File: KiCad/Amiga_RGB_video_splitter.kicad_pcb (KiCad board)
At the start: 4 copper layers, 57.5 x 60 mm, 15 parts, among them J1 DB23_Female-Connector, J2 DB15_Female_HighDensity_Mount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, J3 KMDGX-9S-BS-1, J4 PJ-320A, U1 THS7374IPWR, U2 74HCT2G17

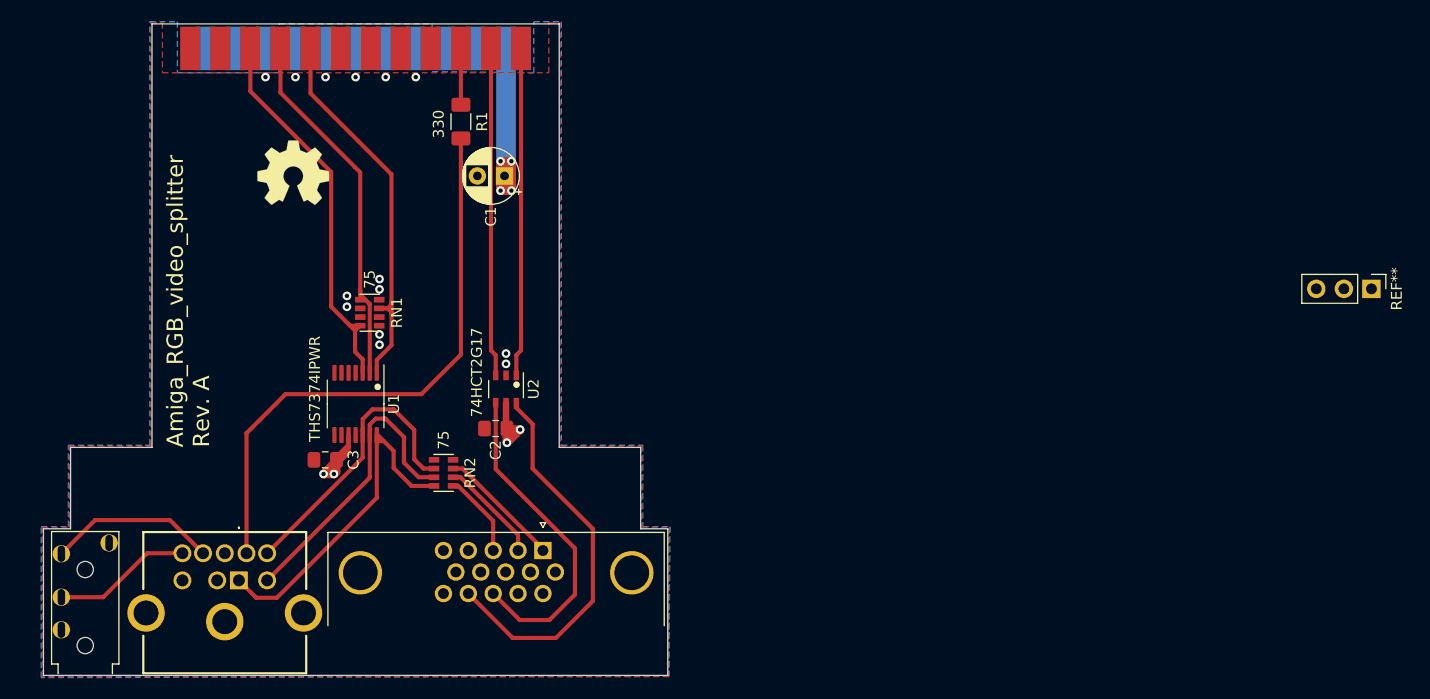
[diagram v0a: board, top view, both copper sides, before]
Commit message: Add 10k pull-up resistor R2 for BYPASS signal going to MSS22D18 3-Pin slide toggle switch
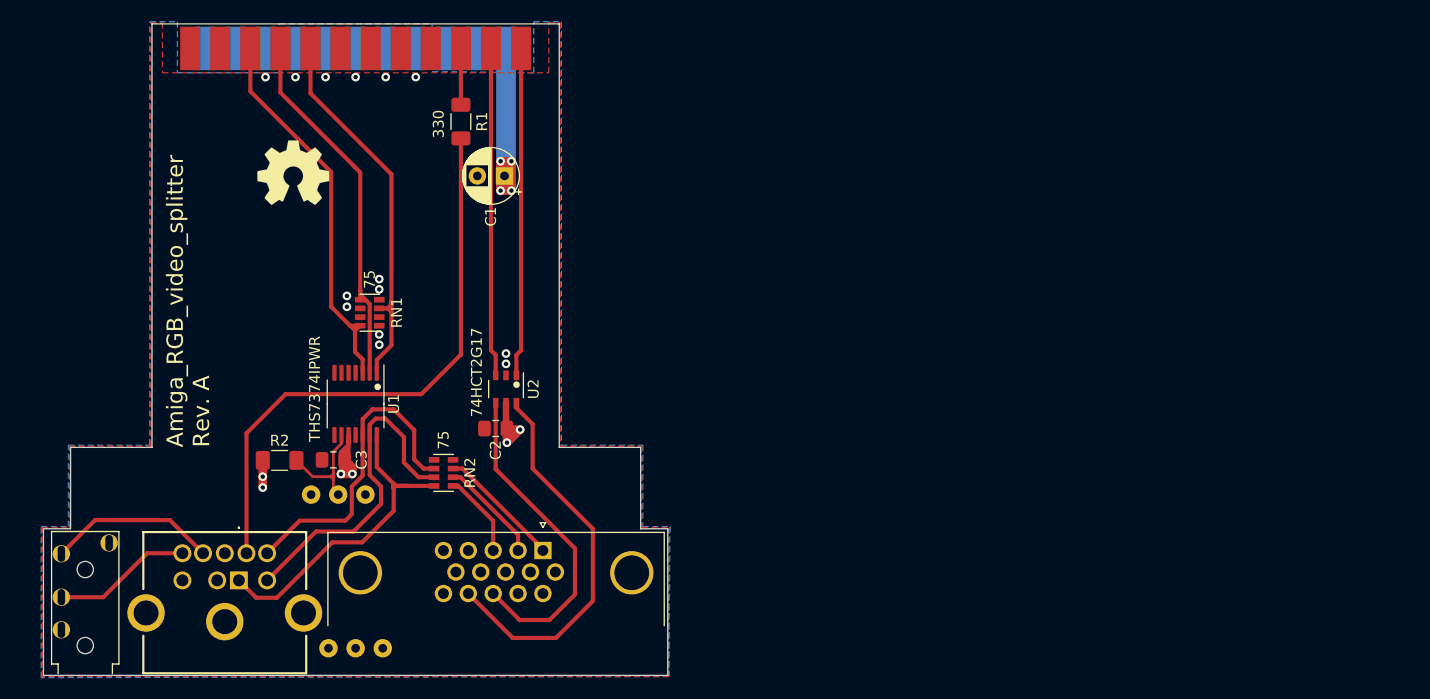
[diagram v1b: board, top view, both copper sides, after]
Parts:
- removed the REF** at (241.2, 109.4)
- added J5: Conn_01x03, Amiga_RGB_video_splitter:PinHeader_1x03_P2.5mm_Vertical, B.Cu at (147.7, 142.5)
- added J5: Conn_01x03, Amiga_RGB_video_splitter:PinHeader_1x03_P2.5mm_Vertical, F.Cu at (146.1, 128.3)
- added R2: 10k, Resistor_SMD:R_1206_3216Metric_Pad1.30x1.75mm_HandSolder, F.Cu at (140.7, 125.2)
- R1: value R_Small -> 330
- moved C3 0.75 mm to (145.7, 125.2)
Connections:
- U1 pad 9: BYPASS -> /BYPASS
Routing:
- net /BYPASS: track 0.00 -> 10.8 mm
- net GREEN: track 28.0 -> 30.9 mm
- net VCC: track 82.5 -> 85.0 mm, vias 8 -> 10
- net RED: track 26.8 -> 29.2 mm

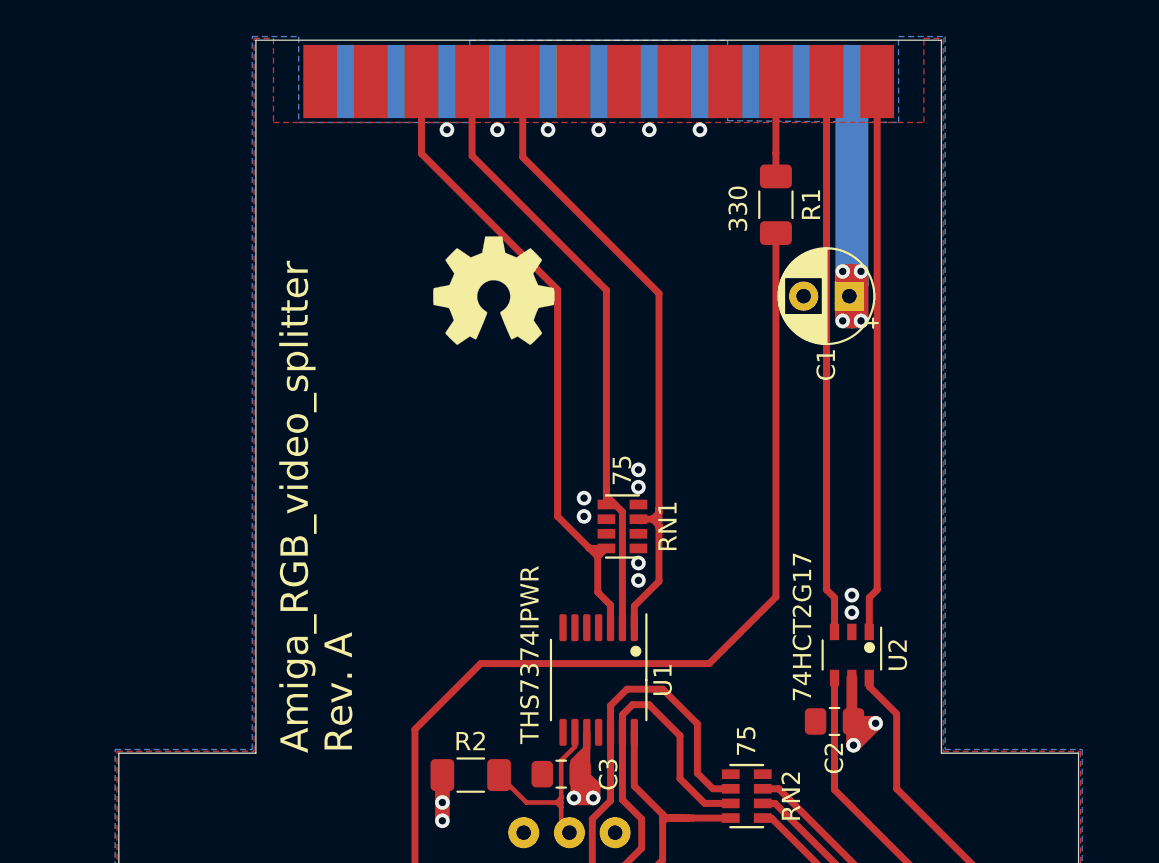
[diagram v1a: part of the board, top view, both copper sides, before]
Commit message: Add U3 (74HCT2G14) and R3,R4,C4,C5 to the design
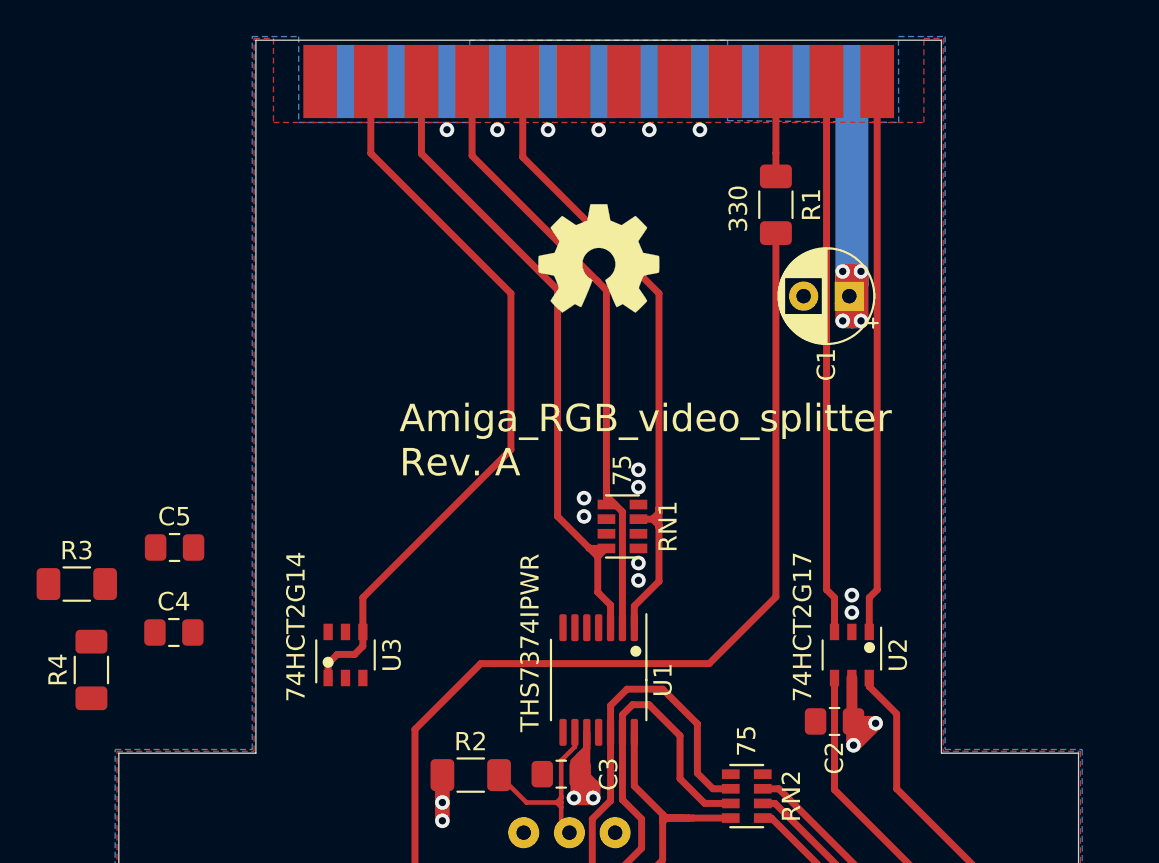
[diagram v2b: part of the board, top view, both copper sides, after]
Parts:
- removed the J5 at (147.7, 142.5)
- added C4: 0.1uF, Capacitor_SMD:C_0805_2012Metric_Pad1.18x1.45mm_HandSolder, F.Cu at (124.5, 117.4)
- added C5: 0.1uF, Capacitor_SMD:C_0805_2012Metric_Pad1.18x1.45mm_HandSolder, F.Cu at (124.5, 112.8)
- added J6: MSS22D18 3Pin Slide Toggle Switch Pitch_2.5mm, Amiga_RGB_video_splitter:PinHeader_1x03_P2.5mm_Vertical, B.Cu at (147.7, 142.5)
- added R3: 10k, Resistor_SMD:R_1206_3216Metric_Pad1.30x1.75mm_HandSolder, F.Cu at (119.2, 114.8)
- added R4: 10k, Resistor_SMD:R_1206_3216Metric_Pad1.30x1.75mm_HandSolder, F.Cu at (120.0, 119.5)
- added U3: 74HCT2G14, Package_SO:TSOP-6_1.65x3.05mm_P0.95mm, F.Cu at (133.8, 118.6)
- J5: value Conn_01x03 -> MSS22D18 3Pin Slide Toggle Switch Pitch_2.5mm
- moved REF** 6.02 mm to (147.7, 97.0)
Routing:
- net XCLKEN: track 0.00 -> 40.5 mm
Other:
- board text added: "74HCT2G14"

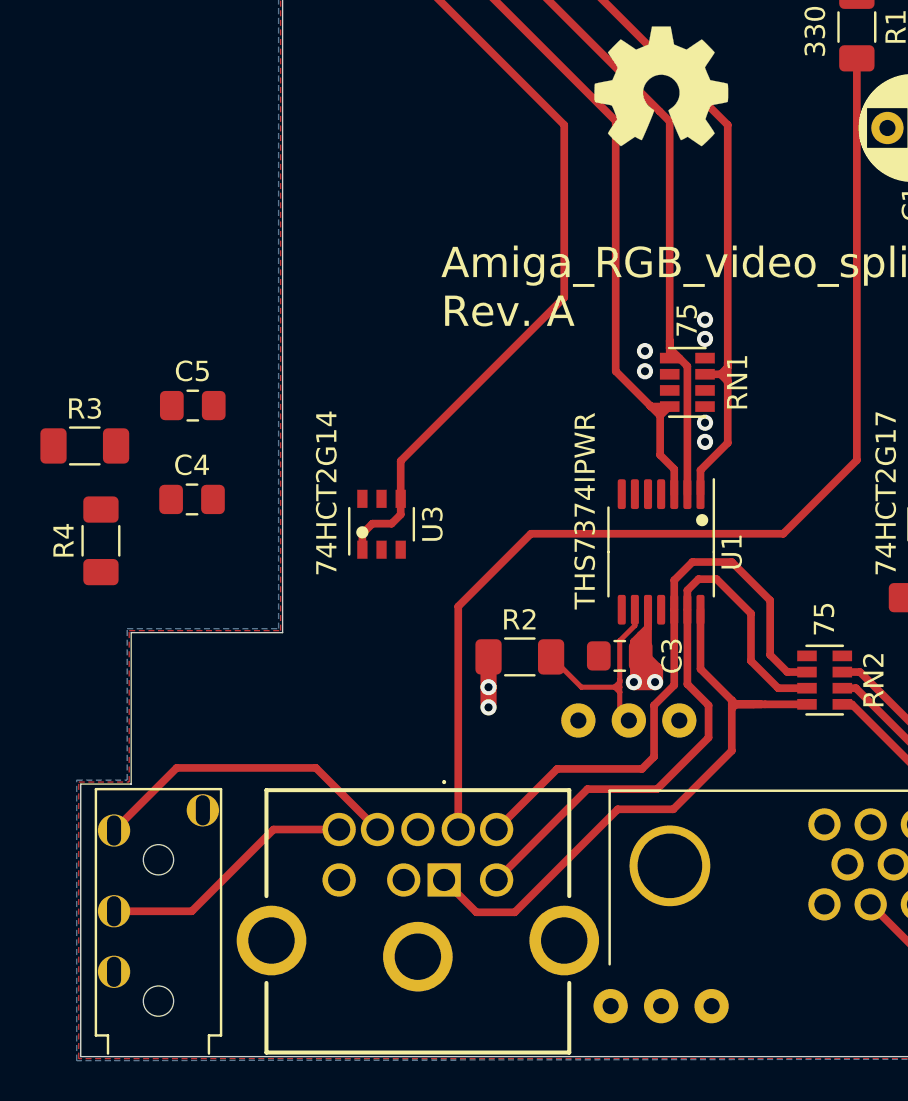
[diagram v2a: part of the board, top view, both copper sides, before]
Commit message: Placement of R3,R4,C4,C5 and routing of U3 circuit
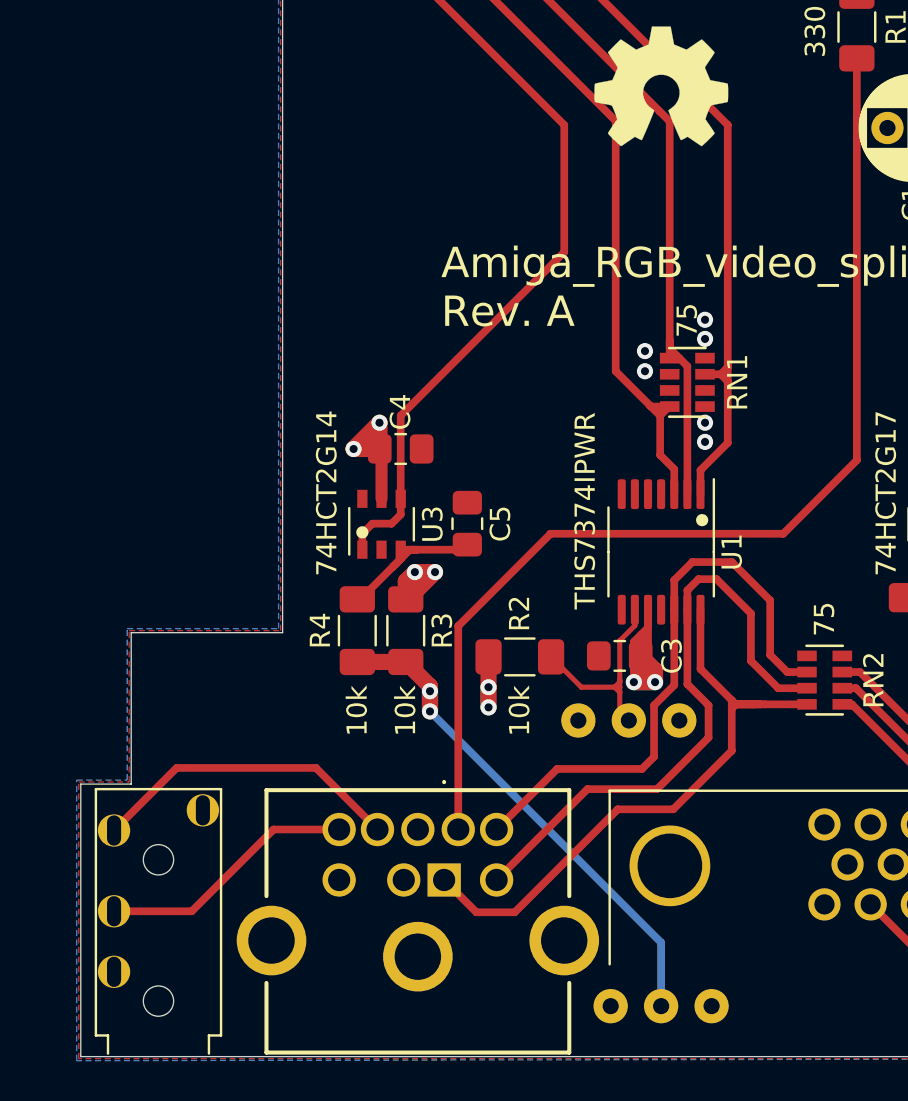
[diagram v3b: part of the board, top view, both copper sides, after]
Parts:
- moved R3 18.3 mm to (135.1, 123.9), turned to 270 degrees
- moved C5 14.8 mm to (138.1, 118.6), turned to 90 degrees
- moved R4 13.5 mm to (132.7, 123.9)
- moved C4 10.6 mm to (134.8, 114.9)
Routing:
- net Net-(J6-Pad2): track 0.00 -> 25.7 mm, vias 0 -> 2
- net VCC: track 85.0 -> 99.6 mm, vias 10 -> 14
- net Net-(C5-Pad1): track 0.00 -> 8.36 mm
- net /CSYNC: track 53.7 -> 53.1 mm
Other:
- board text added: "10k"

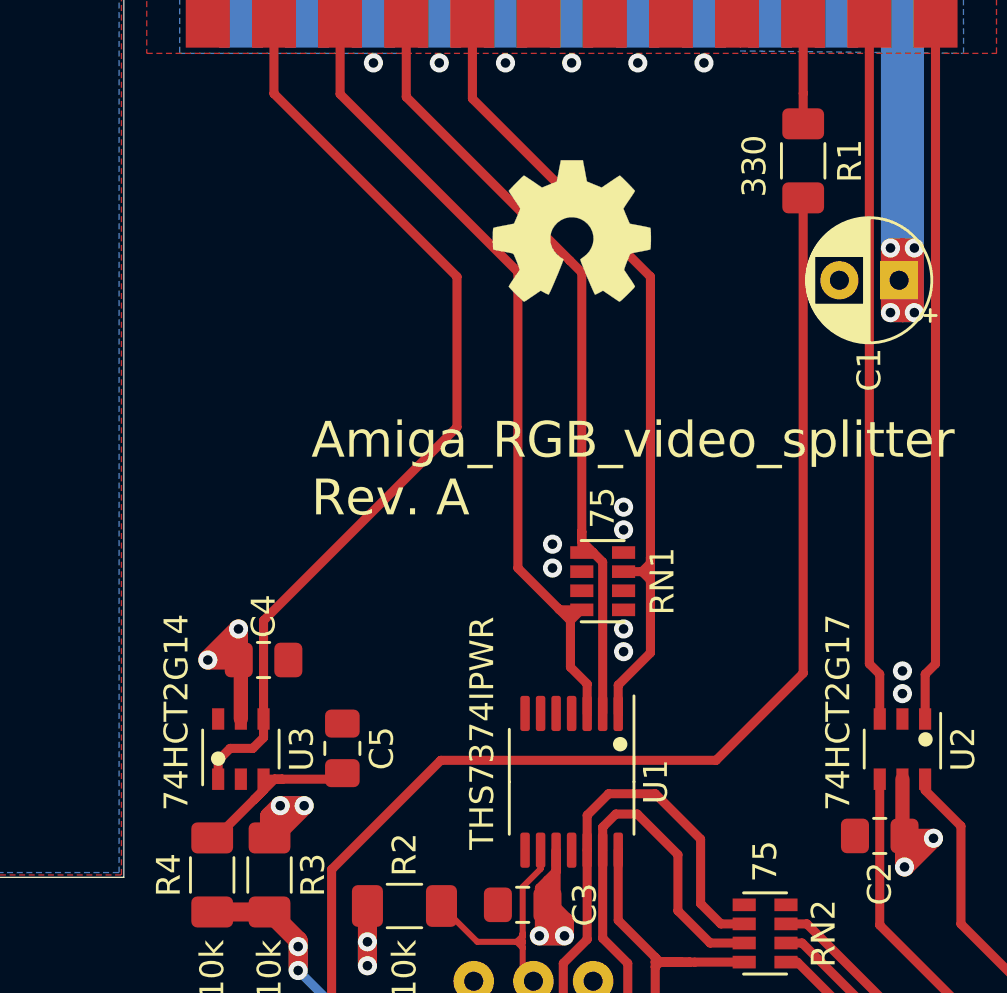
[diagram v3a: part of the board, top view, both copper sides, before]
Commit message: Add U4 (74LVC1GX04) to the design
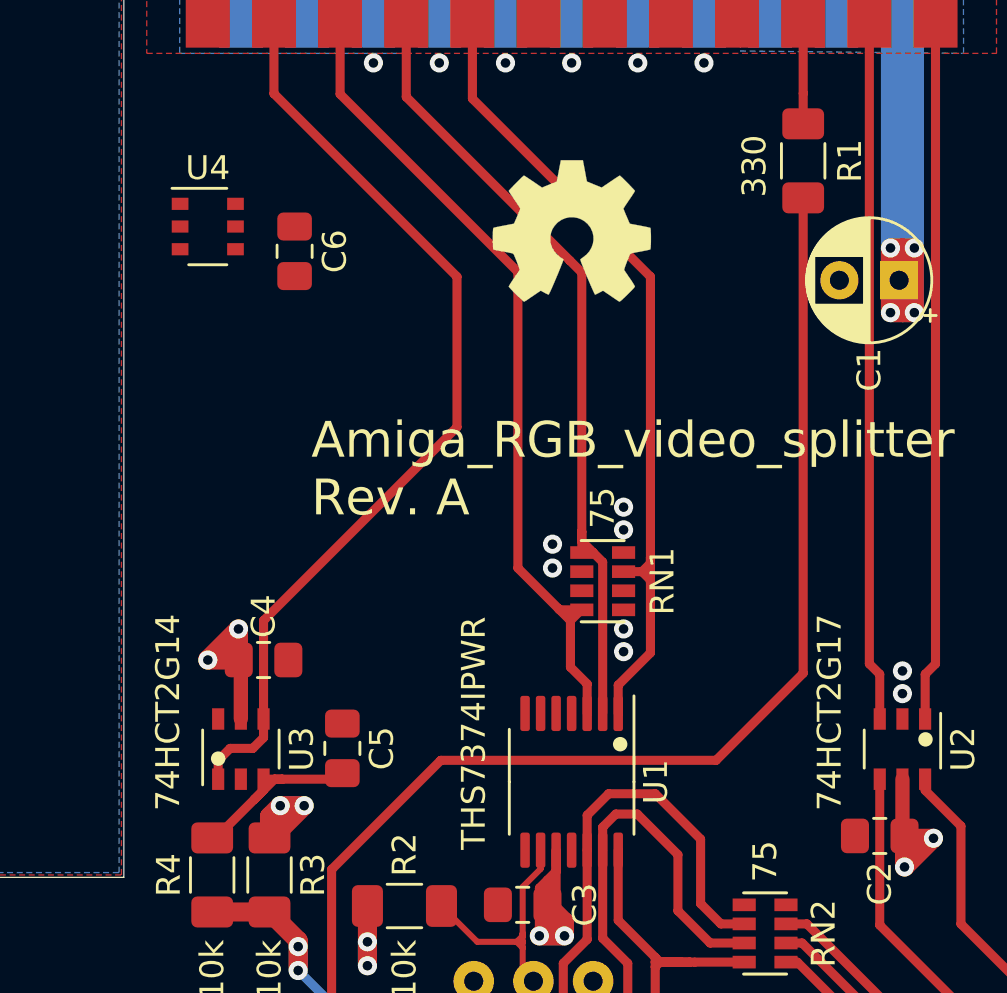
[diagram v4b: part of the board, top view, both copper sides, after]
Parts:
- added C6: 0.1uF, Capacitor_SMD:C_0805_2012Metric_Pad1.18x1.45mm_HandSolder, F.Cu at (136.1, 97.8)
- added U4: 74LVC1GX04, Package_SO:TSOP-6_1.65x3.05mm_P0.95mm, F.Cu at (132.5, 96.8)

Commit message: Placement and routing of U4 (74LVC1GX04)
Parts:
- added R5: 2.2M, Resistor_SMD:R_0603_1608Metric_Pad0.98x0.95mm_HandSolder, F.Cu at (134.2, 99.2)
- moved C6 1.70 mm to (137.8, 97.8)
- moved U4 1.69 mm to (134.2, 96.8)
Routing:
- net XCLK: track 0.00 -> 9.76 mm
- net VCC: track 99.6 -> 102.0 mm
- net Net-(R5-Pad1): track 0.00 -> 1.69 mm
- net Net-(R5-Pad2): track 0.00 -> 1.69 mm
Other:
- board text added: "74LVC1GX04"

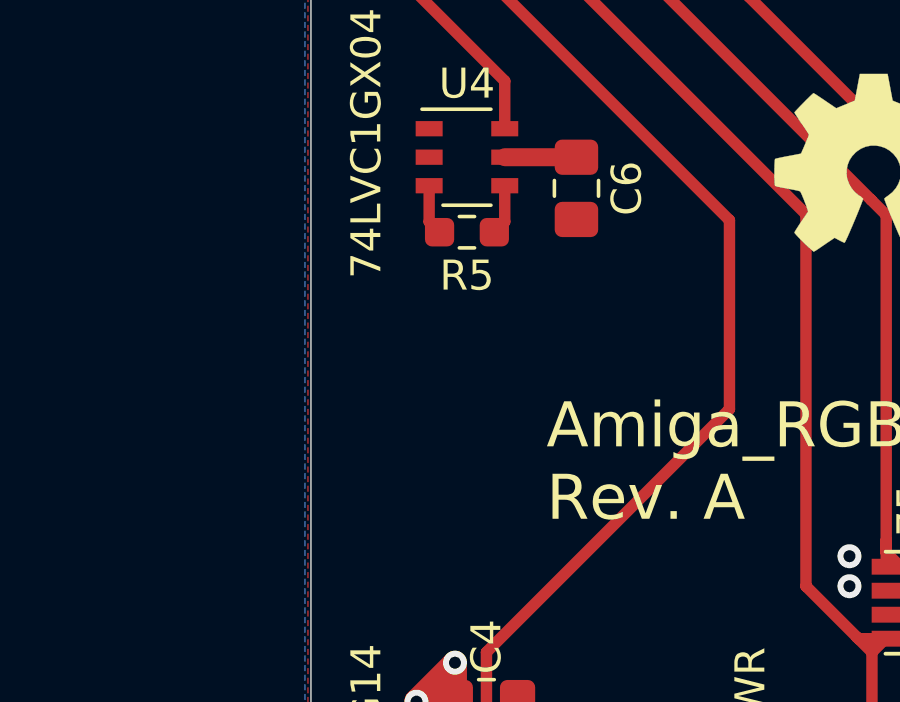
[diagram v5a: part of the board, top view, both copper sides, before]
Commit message: Add Y1 crystal to the design
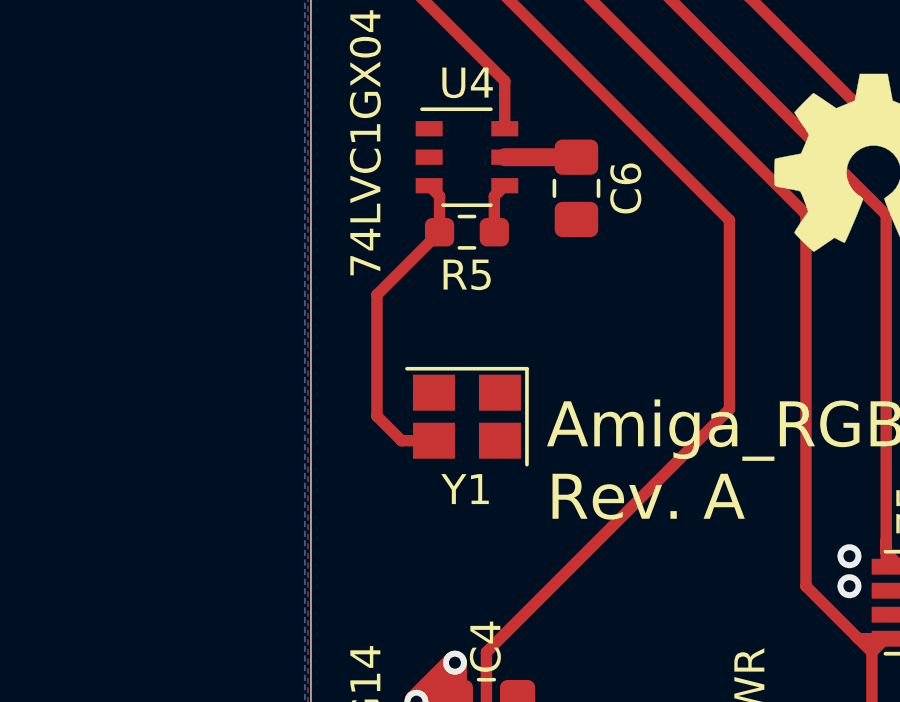
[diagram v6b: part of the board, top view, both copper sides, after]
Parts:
- added Y1: CL=16pF, Crystal:Crystal_SMD_SeikoEpson_FA238-4Pin_3.2x2.5mm, F.Cu at (134.2, 105.4)
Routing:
- net Net-(R5-Pad1): track 1.69 -> 10.9 mm
